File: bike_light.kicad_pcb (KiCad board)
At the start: 4 copper layers, 153.5 x 39.8 mm, 194 parts, among them P1 CONN_6_RA_MALE, P10 CONN_2, P11 CONN_2, P12 CONN_2, P13 CONN_2, P14 CONN_2, P15 CONN_2, P16 CONN_2, P2 CONN_2x2_MALE_RA, P3 CONN_2x2_MALE_RA, P4 CONN_2x2_FEMALE_BACK, P5 CONN_6_FEMALE_FRONT, P6 CONN_2x2_FEMALE_BACK, P7 CONN_2, P8 CONN_2, P9 CONN_2, Q1 AON7611, Q2 DMN65D8L, Q4 DMN65D8L, Q5 DMN65D8L, Q6 DMN65D8L, Q7 DMN65D8L, Q8 DMN65D8L, Q9 DMN65D8L, U1 TEST_PT, U10 TEST_PT, U11 TEST_PT, U12 TEST_PT, U13 TEST_PT, U14 TEST_PT, U15 TEST_PT, U16 TEST_PT, U17 TEST_PT, U18 TEST_PT, U19 TEST_PT, U2 TEST_PT, U20 MCP6L02, U21 74LVC2G06, U22 TPS3700, U23 NC7WZ08, U3 TEST_PT, U30 MSP430G2203IPW28, U31 BH1620FVC, U32 MMA7660FC, U33 AT42QT1011, U34 TOUCHPAD, U35 AT42QT1011, U36 TOUCHPAD, U37 AT42QT1011, U38 TOUCHPAD, U39 TLC59108IPWR, U4 TEST_PT, U40 TLC59108IPWR, U41 TLC59108IPWR, U42 TPS62090, U43 LM3668, U44 CONN_JTAG_14_2_wire, U45 CP2110, U46 ESDR0502N, U47 CONN_USB, U48 BQ24190, U5 TEST_PT, U6 TEST_PT, U7 TEST_PT, U8 TEST_PT, U9 TEST_PT

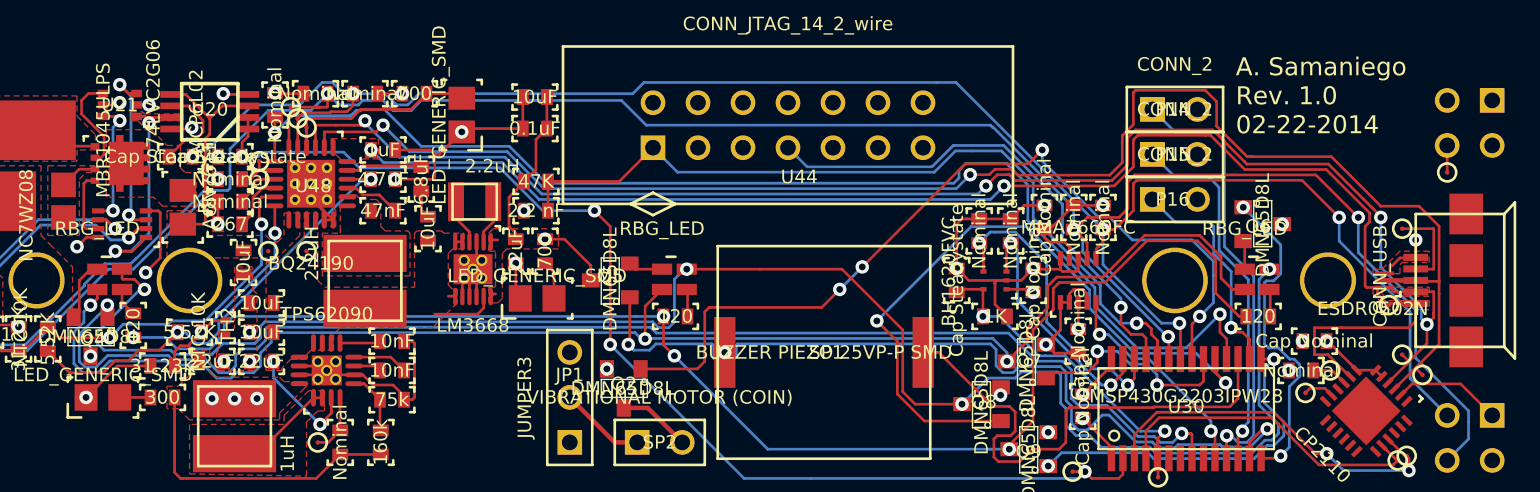
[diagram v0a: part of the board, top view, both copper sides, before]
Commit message: made minor revisions for manufacture
just need to panelize, double check parts, and order
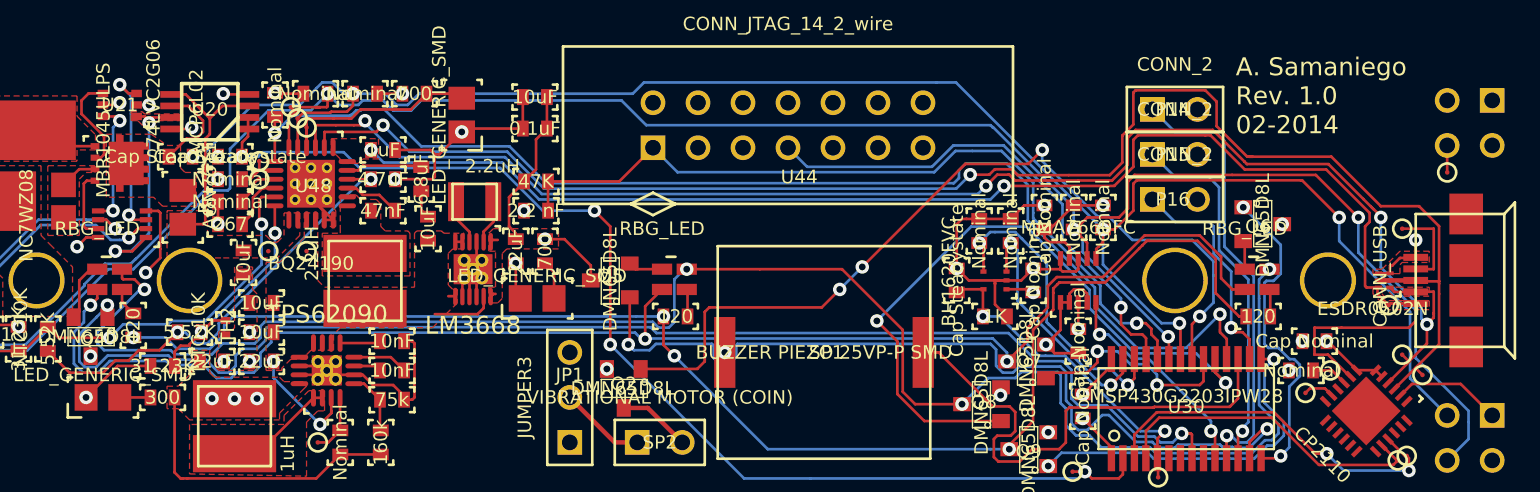
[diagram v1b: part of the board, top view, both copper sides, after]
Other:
- board text added: "A. Samaniego Rev. 1.0 02-2014"
- board text removed: "A. Samaniego Rev. 1.0 02-22-2014"

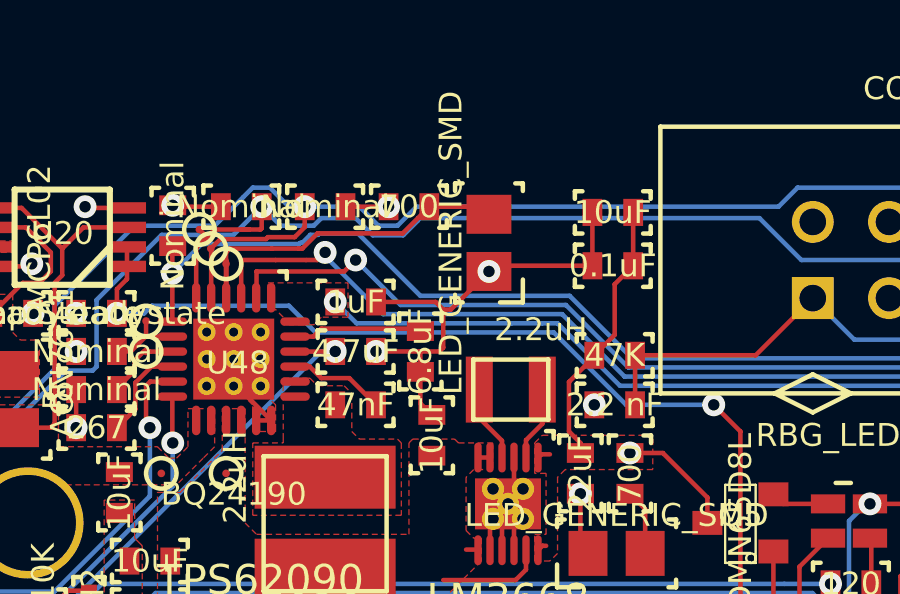
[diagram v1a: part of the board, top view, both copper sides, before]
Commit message: found error in schematic, charger stat LED
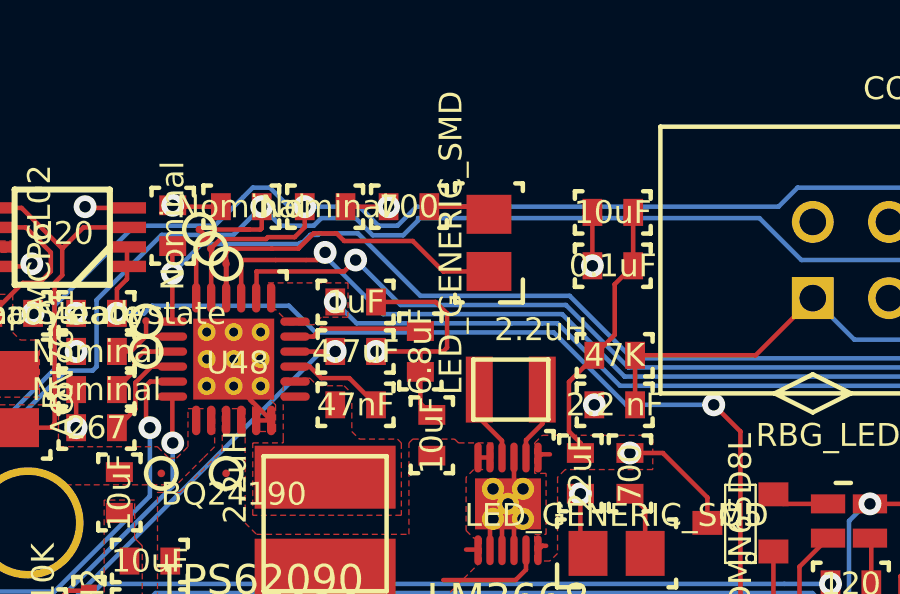
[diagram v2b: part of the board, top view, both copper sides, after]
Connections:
- D38 pad 1: /battery_charger/STATUS -> N-00000102
- D38 pad 2: AGND -> /battery_charger/STATUS
- R48 pad 2: /battery_charger/STATUS -> N-00000102
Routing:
- net AGND: track 222.6 -> 217.2 mm
- net N-00000102: track 0.00 -> 2.09 mm
- added copper zone on F.Cu, net N-00000196
- removed copper zone on F.Cu, net N-00000197
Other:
- board text added: "Solar Panel"

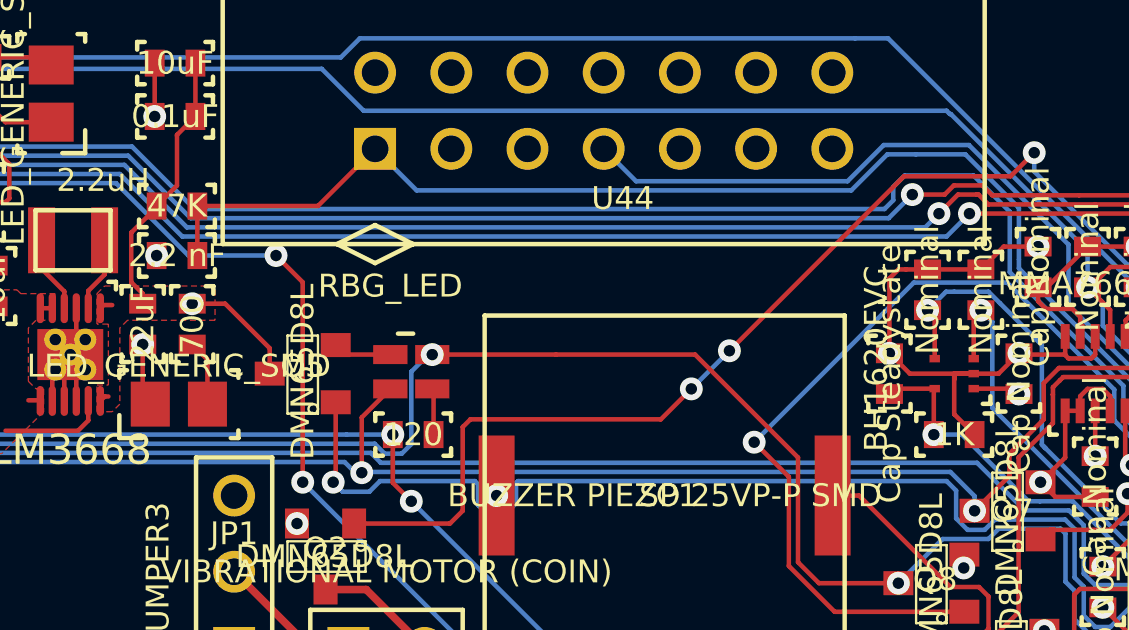
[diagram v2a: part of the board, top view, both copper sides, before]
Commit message: added connector for testing solar panel
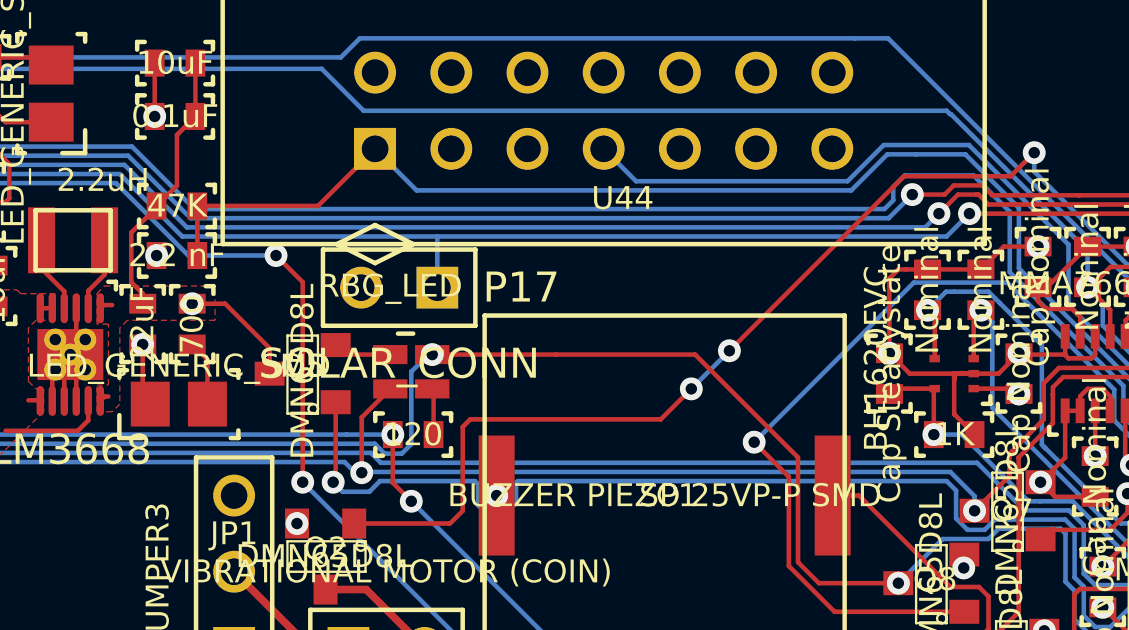
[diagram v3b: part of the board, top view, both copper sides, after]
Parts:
- added P17: SOLAR_CONN, CONN_2x1, F.Cu at (154.6, 80.7)
- turned U17 to 45 degrees
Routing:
- net /battery_charger/USB_5V: track 80.6 -> 82.3 mm
- added copper zone on F.Cu, net N-00000197
- removed copper zone on F.Cu, net N-00000196

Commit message: completed rev 1 of board
need to panelize
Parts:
- added D32: LED_GENERIC_SMD, LED_0805, F.Cu at (163.7, 80.4)
- added D33: DIODESCH, SMini2-F5-B, F.Cu at (161.9, 80.4)
- added R13: 1.55K, r_0603, F.Cu at (157.4, 80.7)
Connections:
- P17 pad 1: /battery_charger/USB_5V -> /interface_solar/SOLAR(+)
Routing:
- net N-00000188: track 0.00 -> 6.32 mm
- net /interface_solar/SOLAR(+): track 0.00 -> 5.74 mm
- net /micro_proc/VIBRATOR: track 48.1 -> 49.2 mm
- net /battery_charger/USB_5V: track 82.3 -> 82.0 mm, vias 2 -> 3
- net AGND: vias 28 -> 29
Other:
- board text added: "2.5V"
- board text added: "3.3V"
